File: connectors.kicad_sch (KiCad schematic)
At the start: 53 parts, among them J1 Molex_Nano-Fit_1x2_SMD_105430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, J2 Conn_FAKRA_59S2AQ-40MT5-Z_1, J3 Conn_FAKRA_59S2AQ-40MT5-Z_1, J4 Conn_FAKRA_59S2AQ-40MT5-Z_1, J5 Conn_FAKRA_59S2AQ-40MT5-Z_1, J6 Conn_FFC_WE_68715014522, U1 SN74LV1T125DBVR, U2 SN74LV1T125DBVR, U8 NTS0102_TSSOP

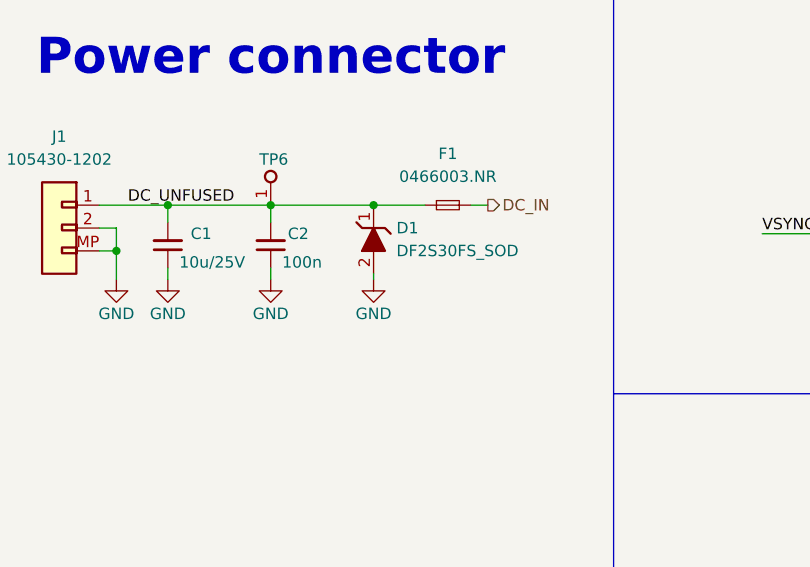
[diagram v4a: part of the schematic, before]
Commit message: Connectors: replace DC connectors' TVS diode
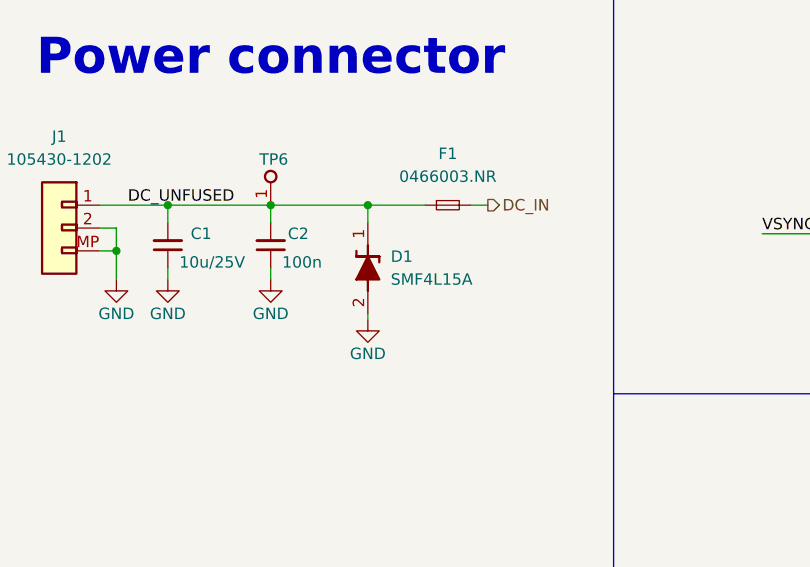
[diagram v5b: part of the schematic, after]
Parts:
- removed D1: DF2S30FS_SOD, antmicro-footprints:SOD-923, symbol antmicroTVSDiodes:DF2S30FS_SOD
- added D1: SMF4L15A, antmicro-footprints:SOD-123FL, symbol antmicroTVSDiodes:SMF4L15A
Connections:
- net DC_UNFUSED: now also D1.1
- net GND: now also D1.2
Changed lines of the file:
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@@
   (junction (at 313.69 177.165) (diameter 0) (color 0 0 0 0)
   )
-  (junction (at 63.5 68.58) (diameter 0) (color 0 0 0 0)
-  )
   (junction (at 348.615 106.045) (diameter 0) (color 0 0 0 0)
   )
@@
   (junction (at 150.495 257.175) (diameter 0) (color 0 0 0 0)
   )
+  (junction (at 62.865 68.58) (diameter 0) (color 0 0 0 0)
+  )
   (junction (at 175.26 114.3) (diameter 0) (color 0 0 0 0)
   )
@@
     (stroke (width 0) (type default) (color 0 0 0 0))
   )
-  (wire (pts (xy 63.5 76.835) (xy 63.5 76.2))
+  (wire (pts (xy 62.865 81.28) (xy 62.865 80.645))
     (stroke (width 0) (type default) (color 0 0 0 0))
   )
@@
     (stroke (width 0) (type default) (color 0 0 0 0))
   )
-  (wire (pts (xy 63.5 68.58) (xy 69.215 68.58))
+  (wire (pts (xy 52.07 68.58) (xy 62.865 68.58))
     (stroke (width 0) (type default) (color 0 0 0 0))
   )
@@
     (stroke (width 0) (type default) (color 0 0 0 0))
   )
+  (wire (pts (xy 62.865 68.58) (xy 69.215 68.58))
+    (stroke (width 0) (type default) (color 0 0 0 0))
+  )
   (wire (pts (xy 329.565 194.945) (xy 329.565 201.93))
     (stroke (width 0) (type default) (color 0 0 0 0))
@@
     (stroke (width 0) (type default) (color 0 0 0 0))
   )
-  (wire (pts (xy 52.07 68.58) (xy 63.5 68.58))
-    (stroke (width 0) (type default) (color 0 0 0 0))
-  )
   (wire (pts (xy 117.475 133.985) (xy 127 133.985))
     (stroke (width 0) (type default) (color 0 0 0 0))
@@
     (stroke (width 0) (type default) (color 0 0 0 0))
   )
+  (wire (pts (xy 62.865 68.58) (xy 62.865 70.485))
+    (stroke (width 0) (type default) (color 0 0 0 0))
+  )
   (wire (pts (xy 120.65 124.46) (xy 120.65 125.095))
     (stroke (width 0) (type default) (color 0 0 0 0))
@@
     (pin "2")
   )
-  (symbol (lib_id "antmicroTVSDiodes:DF2S30FS_SOD") (at 63.5 76.2 90) (unit 1)
-    (in_bom yes) (on_board yes)
-    (property "Reference" "D1" (id 0) (at 66.04 71.12 90)
-      (effects (font (size 1.27 1.27) (thickness 0.15)) (justify right))
-    )
-    (property "Value" "DF2S30FS_SOD" (id 1) (at 66.04 73.66 90)
-      (effects (font (size 1.27 1.27) (thickness 0.15)) (justify right))
-    )
-    (property "Footprint" "antmicro-footprints:SOD-923" (id 2) (at 71.12 54.61 0)
-      (effects (font (size 1.27 1.27) (thickness 0.15)) (justify left bottom) hide)
-    )
-    (property "Datasheet" "https://www.mouser.com/datasheet/2/408/DF2S30FS_datasheet_en_20211216-1916197.pdf" (id 3) (at 73.66 54.61 0)
-      (effects (font (size 1.27 1.27) (thickness 0.15)) (justify left bottom) hide)
-    )
-    (property "Manufacturer" "Toshiba" (id 4) (at 76.2 54.61 0)
-      (effects (font (size 1.27 1.27) (thickness 0.15)) (justify left bottom) hide)
-    )
-    (property "MPN" "DF2S30FS" (id 5) (at 78.74 54.61 0)
-      (effects (font (size 1.27 1.27) (thickness 0.15)) (justify left bottom) hide)
-    )
-    (property "Author" "Antmicro" (id 6) (at 81.28 54.61 0)
-      (effects (font (size 1.27 1.27) (thickness 0.15)) (justify left bottom) hide)
-    )
-    (property "License" "Apache-2.0" (id 7) (at 83.82 54.61 0)
-      (effects (font (size 1.27 1.27) (thickness 0.15)) (justify left bottom) hide)
-    )
-    (pin "1")
-    (pin "2")
-  )
   (symbol (lib_id "antmicroCoaxialConnectorsRF:Conn_FAKRA_59S2AQ-40MT5-Z_1") (at 153.67 210.185 0) (unit 1)
     (in_bom yes) (on_board yes) (fields_autoplaced)
@@
     (pin "1")
   )
+  (symbol (lib_id "antmicroTVSDiodes:SMF4L15A") (at 62.865 80.645 90) (unit 1)
+    (in_bom yes) (on_board yes) (fields_autoplaced)
+    (property "Reference" "D1" (id 0) (at 65.405 74.2949 90)
+      (effects (font (size 1.27 1.27) (thickness 0.15)) (justify right))
+    )
+    (property "Value" "SMF4L15A" (id 1) (at 65.405 76.8349 90)
+      (effects (font (size 1.27 1.27) (thickness 0.15)) (justify right))
+    )
+    (property "Footprint" "antmicro-footprints:SOD-123FL" (id 2) (at 73.025 53.975 0)
+      (effects (font (size 1.27 1.27) (thickness 0.15)) (justify left bottom) hide)
+    )
+    (property "Datasheet" "https://www.mouser.com/datasheet/2/240/Littelfuse_TVS_Diode_SMF4L_Datasheet_pdf-1665786.pdf" (id 3) (at 75.565 53.975 0)
+      (effects (font (size 1.27 1.27) (thickness 0.15)) (justify left bottom) hide)
+    )
+    (property "MPN" "SMF4L15A" (id 4) (at 78.105 53.975 0)
+      (effects (font (size 1.27 1.27) (thickness 0.15)) (justify left bottom) hide)
+    )
+    (property "Manufacturer" "Infineon" (id 5) (at 80.645 53.975 0)
+      (effects (font (size 1.27 1.27) (thickness 0.15)) (justify left bottom) hide)
+    )
+    (property "Author" "Antmicro" (id 6) (at 83.185 53.975 0)
+      (effects (font (size 1.27 1.27) (thickness 0.15)) (justify left bottom) hide)
+    )
+    (property "License" "Apache-2.0" (id 7) (at 85.725 53.975 0)
+      (effects (font (size 1.27 1.27) (thickness 0.15)) (justify left bottom) hide)
+    )
+    (pin "1")
+    (pin "2")
+  )
   (symbol (lib_id "antmicroResistors0402:R_2k2_0402") (at 127 130.175 90) (unit 1)
     (in_bom yes) (on_board yes)
@@
     (pin "2")
   )
-  (symbol (lib_id "antmicropower:GND") (at 63.5 76.835 0) (unit 1)
+  (symbol (lib_id "antmicropower:GND") (at 62.865 81.28 0) (unit 1)
     (in_bom yes) (on_board yes)
-    (property "Reference" "#PWR0102" (id 0) (at 72.39 79.375 0)
+    (property "Reference" "#PWR0102" (id 0) (at 71.755 83.82 0)
       (effects (font (size 1.27 1.27) (thickness 0.15)) (justify left bottom) hide)
     )
-    (property "Value" "GND" (id 1) (at 63.5 80.645 0)
+    (property "Value" "GND" (id 1) (at 62.865 85.09 0)
       (effects (font (size 1.27 1.27) (thickness 0.15)))
     )
-    (property "Footprint" "" (id 2) (at 72.39 84.455 0)
+    (property "Footprint" "" (id 2) (at 71.755 88.9 0)
       (effects (font (size 1.27 1.27) (thickness 0.15)) (justify left bottom) hide)
     )
-    (property "Datasheet" "" (id 3) (at 72.39 89.535 0)
+    (property "Datasheet" "" (id 3) (at 71.755 93.98 0)
       (effects (font (size 1.27 1.27) (thickness 0.15)) (justify left bottom) hide)
     )
-    (property "Author" "Antmicro" (id 4) (at 72.39 84.455 0)
+    (property "Author" "Antmicro" (id 4) (at 71.755 88.9 0)
       (effects (font (size 1.27 1.27) (thickness 0.15)) (justify left bottom) hide)
     )
-    (property "License" "Apache-2.0" (id 5) (at 72.39 86.995 0)
+    (property "License" "Apache-2.0" (id 5) (at 71.755 91.44 0)
       (effects (font (size 1.27 1.27) (thickness 0.15)) (justify left bottom) hide)
     )

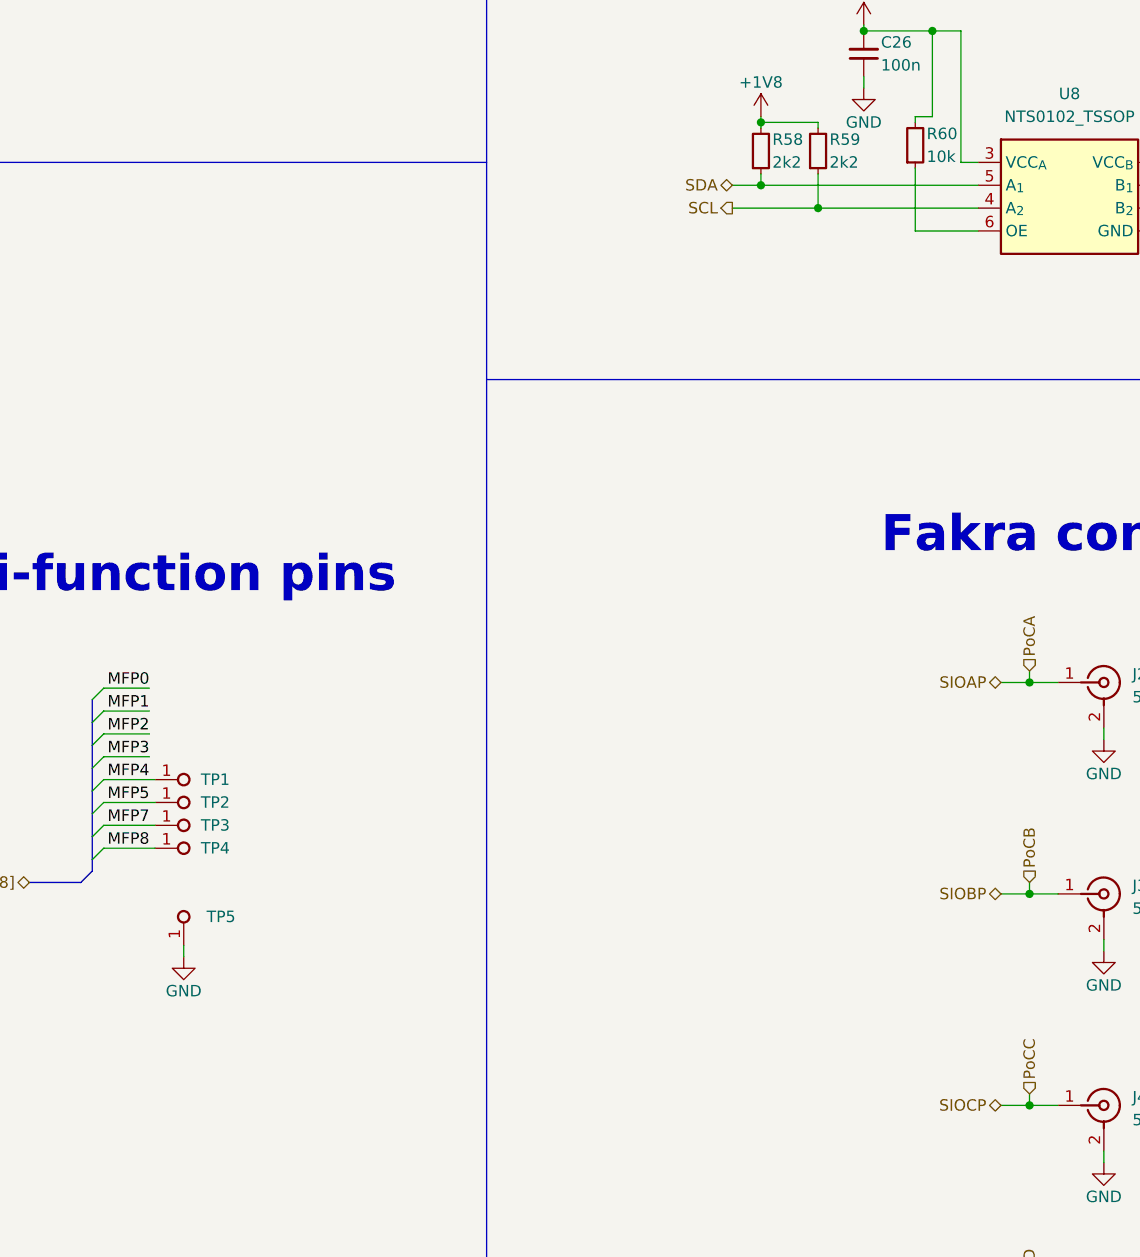
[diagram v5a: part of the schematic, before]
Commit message: Connectors: add optional I2C bus from MFP to level shifter input
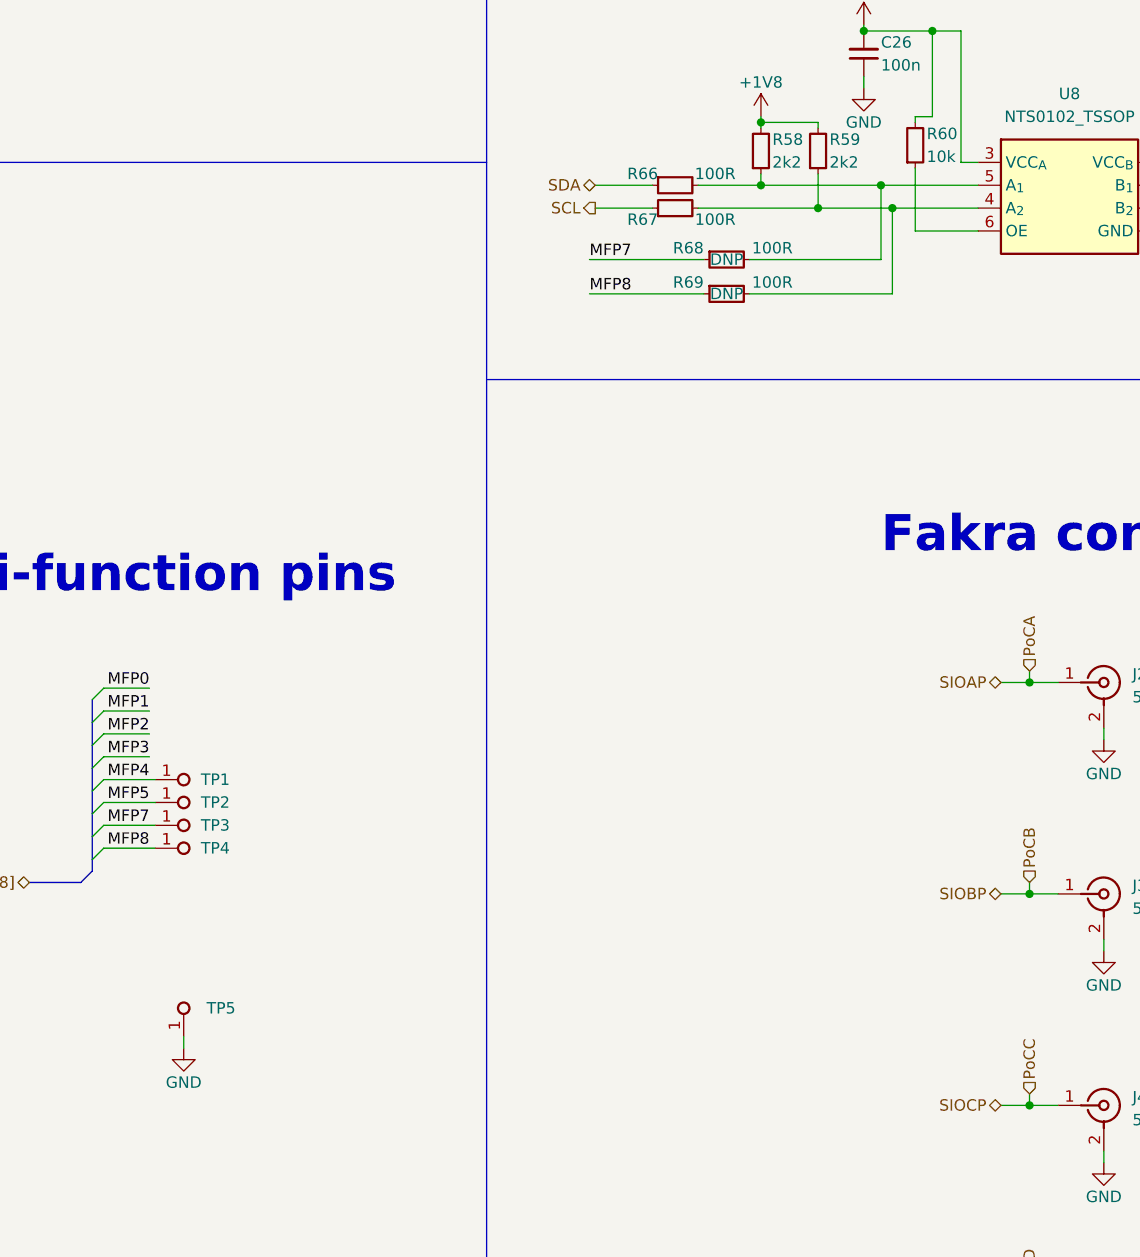
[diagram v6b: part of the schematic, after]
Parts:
- added R66, R67, R68, R69: R_100R_0402, antmicro-footprints:R_0402_1005Metric, symbol antmicroResistors0402:R_100R_0402
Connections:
- net MFP7: now also R68.1
- net MFP8: now also R69.1
- net SCL: now also R67.1; no longer R59.1, U8.4 (A_{2})
- net SDA: now also R66.1; no longer R58.1, U8.5 (A_{1})
- new net: R59.1, R67.2, R69.2, U8.4 (A_{2})
- new net: R58.1, R66.2, R68.2, U8.5 (A_{1})
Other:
- moved on the sheet: TP5

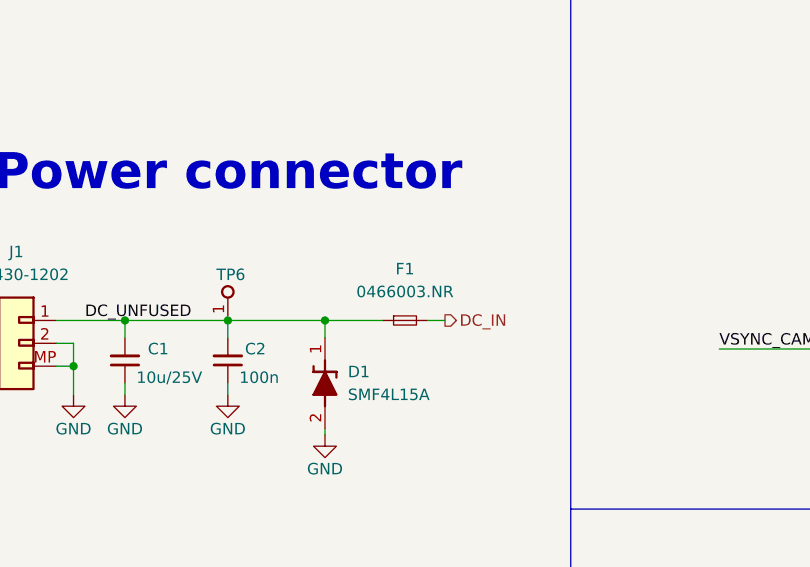
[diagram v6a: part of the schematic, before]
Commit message: Connectors: change fuse to 4A
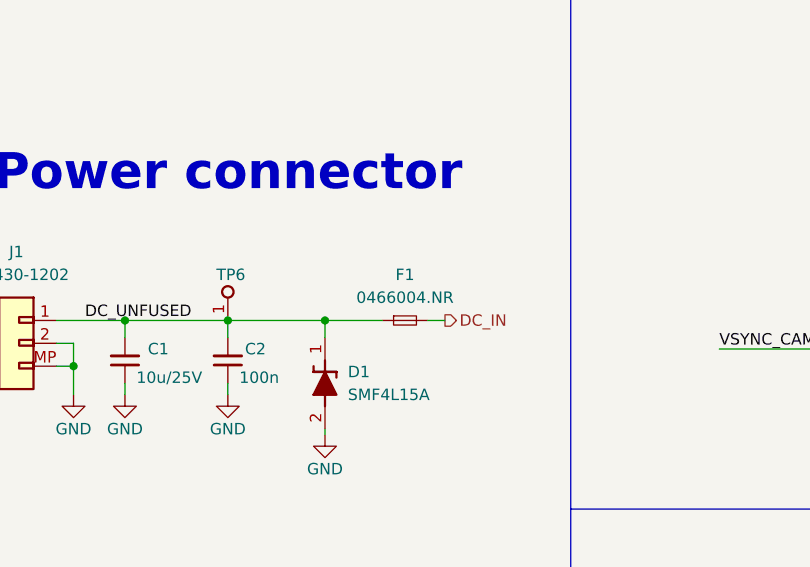
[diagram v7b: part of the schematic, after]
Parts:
- removed F1: F_3A_1206, antmicro-footprints:F_1206_3216Metric, symbol antmicroFuses:F_3A_1206
- added F1: F_4A_1206, antmicro-footprints:F_1206_3216Metric, symbol antmicroFuses:F_4A_1206
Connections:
- net DC_IN: now also F1.2
- net DC_UNFUSED: now also F1.1
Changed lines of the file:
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@@
     (pin "1")
+  )
+  (symbol (lib_id "antmicroFuses:F_4A_1206") (at 69.215 68.58 0) (unit 1)
+    (in_bom yes) (on_board yes) (fields_autoplaced)
+    (property "Reference" "F1" (id 0) (at 71.755 63.5 0)
+      (effects (font (size 1.27 1.27) (thickness 0.15)))
+    )
+    (property "Value" "F_4A_1206" (id 1) (at 89.535 76.2 0)
+      (effects (font (size 1.27 1.27) (thickness 0.15)) (justify left bottom) hide)
+    )
+    (property "Footprint" "antmicro-footprints:F_1206_3216Metric" (id 2) (at 89.535 78.74 0)
+      (effects (font (size 1.27 1.27) (thickness 0.15)) (justify left bottom) hide)
+    )
+    (property "Datasheet" "https://www.littelfuse.com/media?resourcetype=datasheets&itemid=dbe9bcd7-6072-4adf-bf5b-d33e52a6b90f&filename=littelfuse-fuse-466-datasheet" (id 3) (at 89.535 81.28 0)
+      (effects (font (size 1.27 1.27) (thickness 0.15)) (justify left bottom) hide)
+    )
+    (property "Manufacturer" "Littelfuse" (id 4) (at 89.535 83.82 0)
+      (effects (font (size 1.27 1.27) (thickness 0.15)) (justify left bottom) hide)
+    )
+    (property "MPN" "0466004.NR " (id 5) (at 71.755 66.04 0)
+      (effects (font (size 1.27 1.27) (thickness 0.15)))
+    )
+    (property "Author" "Antmicro" (id 6) (at 89.535 88.9 0)
+      (effects (font (size 1.27 1.27) (thickness 0.15)) (justify left bottom) hide)
+    )
+    (property "License" "Apache-2.0" (id 7) (at 89.535 91.44 0)
+      (effects (font (size 1.27 1.27) (thickness 0.15)) (justify left bottom) hide)
+    )
+    (pin "1")
+    (pin "2")
   )
   (symbol (lib_id "antmicropower:GND") (at 132.08 120.65 0) (mirror y) (unit 1)
@@
     )
     (pin "1")
-    (pin "2")
-  )
-  (symbol (lib_id "antmicroFuses:F_3A_1206") (at 69.215 68.58 0) (unit 1)
-    (in_bom yes) (on_board yes) (fields_autoplaced)
-    (property "Reference" "F1" (id 0) (at 71.755 62.865 0)
-      (effects (font (size 1.27 1.27) (thickness 0.15)))
-    )
-    (property "Value" "F_3A_1206" (id 1) (at 89.535 76.2 0)
-      (effects (font (size 1.27 1.27) (thickness 0.15)) (justify left bottom) hide)
-    )
-    (property "Footprint" "antmicro-footprints:F_1206_3216Metric" (id 2) (at 89.535 78.74 0)
-      (effects (font (size 1.27 1.27) (thickness 0.15)) (justify left bottom) hide)
-    )
-    (property "Datasheet" "https://www.littelfuse.com/~/media/electronics/datasheets/fuses/littelfuse_fuse_466_datasheet.pdf.pdf" (id 3) (at 89.535 81.28 0)
-      (effects (font (size 1.27 1.27) (thickness 0.15)) (justify left bottom) hide)
-    )
-    (property "Manufacturer" "Littelfuse" (id 4) (at 89.535 83.82 0)
-      (effects (font (size 1.27 1.27) (thickness 0.15)) (justify left bottom) hide)
-    )
-    (property "MPN" "0466003.NR " (id 5) (at 71.755 65.405 0)
-      (effects (font (size 1.27 1.27) (thickness 0.15)))
-    )
-    (property "Author" "Antmicro" (id 6) (at 89.535 88.9 0)
-      (effects (font (size 1.27 1.27) (thickness 0.15)) (justify left bottom) hide)
-    )
-    (property "License" "Apache-2.0" (id 7) (at 89.535 91.44 0)
-      (effects (font (size 1.27 1.27) (thickness 0.15)) (justify left bottom) hide)
-    )
-    (pin "1")
